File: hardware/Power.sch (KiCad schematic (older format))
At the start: 31 parts, among them J8 Batt, Q10 AO3401A, Q11 AO3400 (A09T), Q12 AO3401A, Q13 AO3400 (A09T), Q14 AO3400 (A09T), Q9 AO3400 (A09T), SW17 SW_SPDT, U1 TP4056, U3 DW-01, U8 HX9193-33GB

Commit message: Added dnp for battery charge circuit
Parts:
- C15, D17, D18, J8, Q10, Q11, Q12, Q13, Q14, Q9, R47, R48, R49, R50, R51, R52, R53, R54, R55, R56, R57, R58, SW17, U1, U3: dnp (none) -> y
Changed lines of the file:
@@
 F 8 "DW01" H 6700 4050 50  0001 L BNN "Field8"
 F 9 "C14213" H 6700 4050 50  0001 C CNN "LCSC"
+F 10 "y" H 6700 4050 50  0001 C CNN "dnp"
 	1    6700 4050
 	1    0    0    -1
@@
 F 3 "~" H 5800 3800 50  0001 C CNN
 F 4 "C23179" H 5800 3800 50  0001 C CNN "LCSC"
+F 5 "y" H 5800 3800 50  0001 C CNN "dnp"
 	1    5800 3800
 	0    1    1    0
@@
 F 3 "~" H 6150 3950 50  0001 C CNN
 F 4 "C14663" H 6150 3950 50  0001 C CNN "LCSC"
+F 5 "y" H 6150 3950 50  0001 C CNN "dnp"
 	1    6150 3950
 	1    0    0    -1
@@
 F 3 "http://www.aosmd.com/pdfs/datasheet/ao3400.pdf" H 6450 4850 50  0001 L CNN
 F 4 "C20917" H 6450 4850 50  0001 C CNN "LCSC"
+F 5 "y" H 6450 4850 50  0001 C CNN "dnp"
 	1    6450 4850
 	0    1    1    0
@@
 F 3 "http://www.aosmd.com/pdfs/datasheet/ao3400.pdf" H 6900 4850 50  0001 L CNN
 F 4 "C20917" H 6900 4850 50  0001 C CNN "LCSC"
+F 5 "y" H 6900 4850 50  0001 C CNN "dnp"
 	1    6900 4850
 	0    -1   1    0
@@
 F 3 "~" H 7200 4350 50  0001 C CNN
 F 4 "C21190" H 7200 4350 50  0001 C CNN "LCSC"
+F 5 "y" H 7200 4350 50  0001 C CNN "dnp"
 	1    7200 4350
 	-1   0    0    1
@@
 F 3 "http://www.aosmd.com/pdfs/datasheet/AO3401A.pdf" H 5150 2500 50  0001 L CNN
 F 4 "C15127" H 5150 2500 50  0001 C CNN "LCSC"
+F 5 "y" H 5150 2500 50  0001 C CNN "dnp"
 	1    5150 2500
 	0    -1   -1   0
@@
 F 3 "http://www.aosmd.com/pdfs/datasheet/AO3401A.pdf" H 5550 2500 50  0001 L CNN
 F 4 "C15127" H 5550 2500 50  0001 C CNN "LCSC"
+F 5 "y" H 5550 2500 50  0001 C CNN "dnp"
 	1    5550 2500
 	0    1    -1   0
@@
 F 3 "~" H 5000 2700 50  0001 C CNN
 F 4 "C25804" H 5000 2700 50  0001 C CNN "LCSC"
+F 5 "y" H 5000 2700 50  0001 C CNN "dnp"
 	1    5000 2700
 	0    1    -1   0
@@
 F 3 "https://dlnmh9ip6v2uc.cloudfront.net/datasheets/Prototyping/TP4056.pdf" H 3600 4150 60  0001 C CNN
 F 4 "C16581" H 3600 4150 50  0001 C CNN "LCSC"
+F 5 "y" H 3600 4150 50  0001 C CNN "dnp"
 	1    3600 4150
 	1    0    0    -1
@@
 F 3 "~" H 4100 4450 50  0001 C CNN
 F 4 "C22765" H 4100 4450 50  0001 C CNN "LCSC"
+F 5 "y" H 4100 4450 50  0001 C CNN "dnp"
 	1    4100 4450
 	1    0    0    -1
@@
 F 3 "~" H 2550 4600 50  0001 C CNN
 F 4 "C72043" H 2550 4600 50  0001 C CNN "LCSC"
+F 5 "y" H 2550 4600 50  0001 C CNN "dnp"
 	1    2550 4600
 	-1   0    0    1
@@
 F 3 "~" H 2550 4500 50  0001 C CNN
 F 4 "C72043" H 2550 4500 50  0001 C CNN "LCSC"
+F 5 "y" H 2550 4500 50  0001 C CNN "dnp"
 	1    2550 4500
 	-1   0    0    1
@@
 F 3 "~" H 2850 4350 50  0001 C CNN
 F 4 "C25804" H 2850 4350 50  0001 C CNN "LCSC"
+F 5 "y" H 2850 4350 50  0001 C CNN "dnp"
 	1    2850 4350
 	-1   0    0    -1
@@
 F 3 "~" H 3000 4450 50  0001 C CNN
 F 4 "C25804" H 3000 4450 50  0001 C CNN "LCSC"
+F 5 "y" H 3000 4450 50  0001 C CNN "dnp"
 	1    3000 4450
 	1    0    0    -1
@@
 F 3 "~" H 2750 3850 50  0001 C CNN
 F 4 "C25804" H 2750 3850 50  0001 C CNN "LCSC"
+F 5 "y" H 2750 3850 50  0001 C CNN "dnp"
 	1    2750 3850
 	1    0    0    -1
@@
 F 3 "http://www.aosmd.com/pdfs/datasheet/ao3400.pdf" H 2300 3950 50  0001 L CNN
 F 4 "C20917" H 2300 3950 50  0001 C CNN "LCSC"
+F 5 "y" V 2300 3950 50  0001 C CNN "dnp"
 	1    2300 3950
 	0    1    -1   0
@@
 F 3 "~" H 1950 4000 50  0001 C CNN
 F 4 "C25804" H 1950 4000 50  0001 C CNN "LCSC"
+F 5 "y" H 1950 4000 50  0001 C CNN "dnp"
 	1    1950 4000
 	1    0    0    -1
@@
 F 3 "http://www.aosmd.com/pdfs/datasheet/ao3400.pdf" H 5150 4550 50  0001 L CNN
 F 4 "C20917" H 5150 4550 50  0001 C CNN "LCSC"
+F 5 "y" H 5150 4550 50  0001 C CNN "dnp"
 	1    5150 4550
 	-1   0    0    -1
@@
 F 3 "~" H 5450 4200 50  0001 C CNN
 F 4 "C25804" H 5450 4200 50  0001 C CNN "LCSC"
+F 5 "y" H 5450 4200 50  0001 C CNN "dnp"
 	1    5450 4200
 	-1   0    0    1
@@
 F 2 "Connector_JST:JST_PH_B3B-PH-SM4-TB_1x03-1MP_P2.00mm_Vertical" H 4850 4050 50  0001 C CNN
 F 3 "~" H 4850 4050 50  0001 C CNN
+F 4 "y" H 4850 4050 50  0001 C CNN "dnp"
 	1    4850 4050
 	-1   0    0    -1
@@
 F 3 "~" H 4350 4450 50  0001 C CNN
 F 4 "C21189" H 4350 4450 50  0001 C CNN "LCSC"
+F 5 "y" H 4350 4450 50  0001 C CNN "dnp"
 	1    4350 4450
 	1    0    0    -1
@@
 F 2 "Resistor_SMD:R_0603_1608Metric" V 4280 3950 50  0001 C CNN
 F 3 "~" H 4350 3950 50  0001 C CNN
+F 4 "y" H 4350 3950 50  0001 C CNN "dnp"
 	1    4350 3950
 	1    0    0    -1
@@
 F 2 "Resistor_SMD:R_0603_1608Metric" V 4430 4200 50  0001 C CNN
 F 3 "~" H 4500 4200 50  0001 C CNN
+F 4 "y" H 4500 4200 50  0001 C CNN "dnp"
 	1    4500 4200
 	0    1    1    0
@@
 F 2 "switch:sk-3296s" H 5550 3000 50  0001 C CNN
 F 3 "~" H 5550 3000 50  0001 C CNN
+F 4 "y" H 5550 3000 50  0001 C CNN "dnp"
 	1    5550 3000
 	0    1    1    0

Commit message: Value cleanup
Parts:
- U8: value HX9193-33GB -> HX9193-33GB
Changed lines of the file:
@@
 P 9550 5700
 F 0 "U8" H 9550 6067 50  0000 C CNN
-F 1 " HX9193-33GB" H 9550 5976 50  0000 C CNN
+F 1 "HX9193-33GB" H 9550 5976 50  0000 C CNN
 F 2 "Package_TO_SOT_SMD:SOT-23-5" H 9550 5300 50  0001 C CNN
 F 3 "" H 9300 5950 50  0001 C CNN

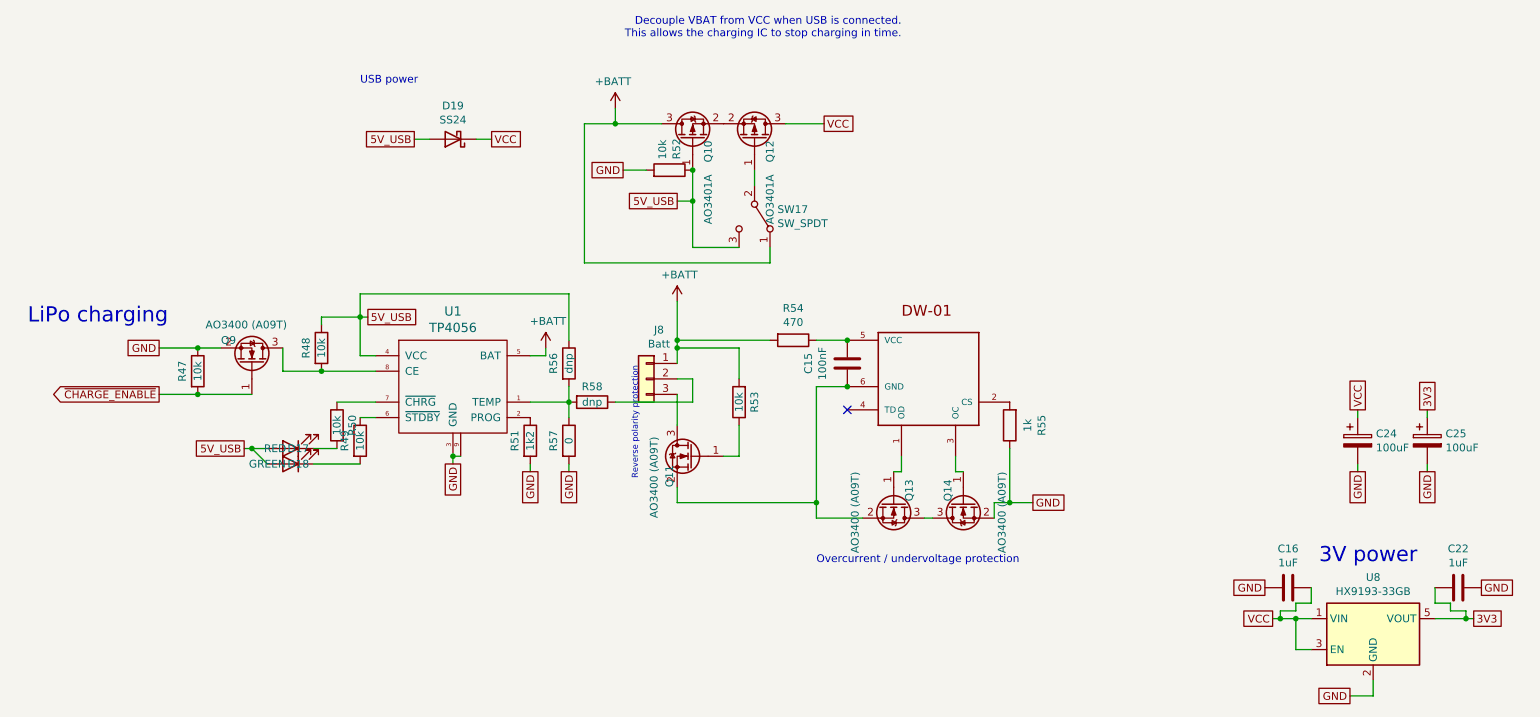
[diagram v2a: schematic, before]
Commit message: Added testpoints to audio lines
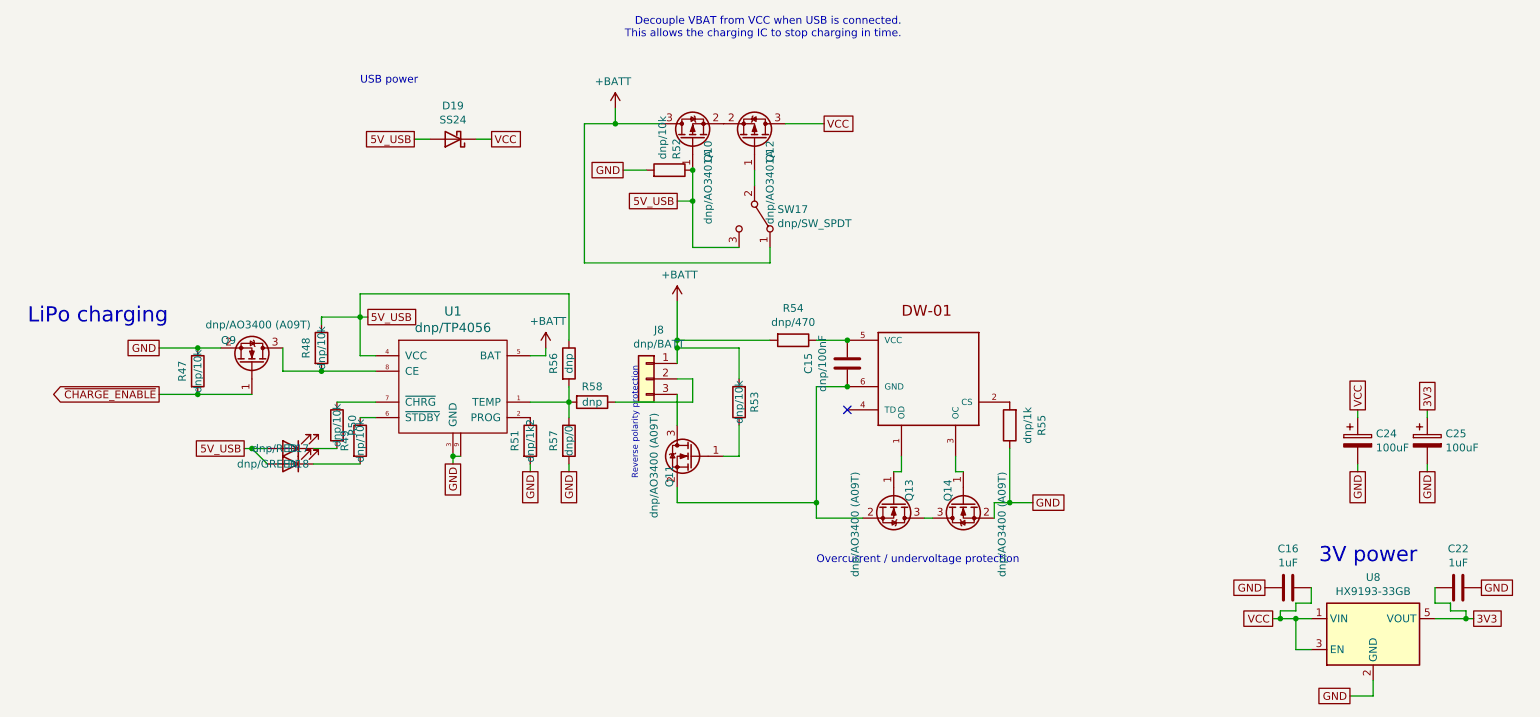
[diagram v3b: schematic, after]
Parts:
- C15: value 100nF -> dnp/100nF; LCSC C14663 -> (none)
- D17: value RED -> dnp/RED; LCSC C72043 -> (none)
- D18: value GREEN -> dnp/GREEN; LCSC C72043 -> (none)
- J8: value Batt -> dnp/BATT
- Q10, Q12: value AO3401A -> dnp/AO3401A; LCSC C15127 -> (none)
- Q11, Q13, Q14, Q9: value AO3400 (A09T) -> dnp/AO3400 (A09T); LCSC C20917 -> (none)
- R47, R48, R49, R50, R52, R53: value 10k -> dnp/10k; LCSC C25804 -> (none)
- R51: value 1k2 -> dnp/1k2; LCSC C22765 -> (none)
- R54: value 470 -> dnp/470; LCSC C23179 -> (none)
- R55: value 1k -> dnp/1k; LCSC C21190 -> (none)
- R57: value 0 -> dnp/0; LCSC C21189 -> (none)
- SW17: value SW_SPDT -> dnp/SW_SPDT
- U1: value TP4056 -> dnp/TP4056; LCSC C16581 -> (none)
- U3: value DW-01 -> dnp/DW-01; LCSC C14213 -> (none)
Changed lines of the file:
@@
 AR Path="/5E464BBE/5E449AD7" Ref="U3"  Part="1"
 F 0 "U3" H 6700 4050 50  0001 L BNN
-F 1 "DW-01" H 6700 4050 50  0001 L BNN
+F 1 "dnp/DW-01" H 6700 4050 50  0001 L BNN
 F 2 "Package_TO_SOT_SMD:SOT-23-6" H 6700 4050 50  0001 L BNN
 F 3 "1808 Murata Electronics" H 6700 4050 50  0001 L BNN
@@
 F 7 "Eldon Vloerstaande kasten DW - DW01" H 6700 4050 50  0001 L BNN "Field7"
 F 8 "DW01" H 6700 4050 50  0001 L BNN "Field8"
-F 9 "C14213" H 6700 4050 50  0001 C CNN "LCSC"
+F 9 "" H 6700 4050 50  0001 C CNN "LCSC"
 F 10 "y" H 6700 4050 50  0001 C CNN "dnp"
 	1    6700 4050
@@
 AR Path="/5E464BBE/5E449ADE" Ref="R54"  Part="1"
 F 0 "R54" V 5593 3800 50  0000 C CNN
-F 1 "470" V 5684 3800 50  0000 C CNN
+F 1 "dnp/470" V 5684 3800 50  0000 C CNN
 F 2 "Resistor_SMD:R_0603_1608Metric" V 5730 3800 50  0001 C CNN
 F 3 "~" H 5800 3800 50  0001 C CNN
-F 4 "C23179" H 5800 3800 50  0001 C CNN "LCSC"
+F 4 "" H 5800 3800 50  0001 C CNN "LCSC"
 F 5 "y" H 5800 3800 50  0001 C CNN "dnp"
 	1    5800 3800
@@
 AR Path="/5E464BBE/5E449AE7" Ref="C15"  Part="1"
 F 0 "C15" V 5898 3950 50  0000 C CNN
-F 1 "100nF" V 5989 3950 50  0000 C CNN
+F 1 "dnp/100nF" V 5989 3950 50  0000 C CNN
 F 2 "Capacitor_SMD:C_0603_1608Metric" H 6188 3800 50  0001 C CNN
 F 3 "~" H 6150 3950 50  0001 C CNN
-F 4 "C14663" H 6150 3950 50  0001 C CNN "LCSC"
+F 4 "" H 6150 3950 50  0001 C CNN "LCSC"
 F 5 "y" H 6150 3950 50  0001 C CNN "dnp"
 	1    6150 3950
@@
 AR Path="/5E464BBE/5E449AEF" Ref="Q13"  Part="1"
 F 0 "Q13" H 6300 4950 50  0000 L CNN
-F 1 "AO3400 (A09T)" H 6250 4600 50  0000 L CNN
+F 1 "dnp/AO3400 (A09T)" H 6250 4600 50  0000 L CNN
 F 2 "Package_TO_SOT_SMD:SOT-23" H 6650 4775 50  0001 L CIN
 F 3 "http://www.aosmd.com/pdfs/datasheet/ao3400.pdf" H 6450 4850 50  0001 L CNN
-F 4 "C20917" H 6450 4850 50  0001 C CNN "LCSC"
+F 4 "" H 6450 4850 50  0001 C CNN "LCSC"
 F 5 "y" H 6450 4850 50  0001 C CNN "dnp"
 	1    6450 4850
@@
 AR Path="/5E464BBE/5E449AF5" Ref="Q14"  Part="1"
 F 0 "Q14" H 6750 4950 50  0000 L CNN
-F 1 "AO3400 (A09T)" H 6700 4600 50  0000 L CNN
+F 1 "dnp/AO3400 (A09T)" H 6700 4600 50  0000 L CNN
 F 2 "Package_TO_SOT_SMD:SOT-23" H 7100 4775 50  0001 L CIN
 F 3 "http://www.aosmd.com/pdfs/datasheet/ao3400.pdf" H 6900 4850 50  0001 L CNN
-F 4 "C20917" H 6900 4850 50  0001 C CNN "LCSC"
+F 4 "" H 6900 4850 50  0001 C CNN "LCSC"
 F 5 "y" H 6900 4850 50  0001 C CNN "dnp"
 	1    6900 4850
@@
 AR Path="/5E464BBE/5E449B1C" Ref="R55"  Part="1"
 F 0 "R55" V 6993 4350 50  0000 C CNN
-F 1 "1k" V 7084 4350 50  0000 C CNN
+F 1 "dnp/1k" V 7084 4350 50  0000 C CNN
 F 2 "Resistor_SMD:R_0603_1608Metric" V 7130 4350 50  0001 C CNN
 F 3 "~" H 7200 4350 50  0001 C CNN
-F 4 "C21190" H 7200 4350 50  0001 C CNN "LCSC"
+F 4 "" H 7200 4350 50  0001 C CNN "LCSC"
 F 5 "y" H 7200 4350 50  0001 C CNN "dnp"
 	1    7200 4350
@@
 AR Path="/5E464BBE/5E45C88D" Ref="Q10"  Part="1"
 F 0 "Q10" H 5000 2400 50  0000 L CNN
-F 1 "AO3401A" H 4600 2400 50  0000 L CNN
+F 1 "dnp/AO3401A" H 4600 2400 50  0000 L CNN
 F 2 "Package_TO_SOT_SMD:SOT-23" H 5350 2425 50  0001 L CIN
 F 3 "http://www.aosmd.com/pdfs/datasheet/AO3401A.pdf" H 5150 2500 50  0001 L CNN
-F 4 "C15127" H 5150 2500 50  0001 C CNN "LCSC"
+F 4 "" H 5150 2500 50  0001 C CNN "LCSC"
 F 5 "y" H 5150 2500 50  0001 C CNN "dnp"
 	1    5150 2500
@@
 AR Path="/5E464BBE/5E45C893" Ref="Q12"  Part="1"
 F 0 "Q12" H 5400 2600 50  0000 L CNN
-F 1 "AO3401A" H 5000 2600 50  0000 L CNN
+F 1 "dnp/AO3401A" H 5000 2600 50  0000 L CNN
 F 2 "Package_TO_SOT_SMD:SOT-23" H 5750 2425 50  0001 L CIN
 F 3 "http://www.aosmd.com/pdfs/datasheet/AO3401A.pdf" H 5550 2500 50  0001 L CNN
-F 4 "C15127" H 5550 2500 50  0001 C CNN "LCSC"
+F 4 "" H 5550 2500 50  0001 C CNN "LCSC"
 F 5 "y" H 5550 2500 50  0001 C CNN "dnp"
 	1    5550 2500
@@
 AR Path="/5E464BBE/5E45C8FB" Ref="R52"  Part="1"
 F 0 "R52" H 5070 2746 50  0000 L CNN
-F 1 "10k" H 5070 2655 50  0000 L CNN
+F 1 "dnp/10k" H 5070 2655 50  0000 L CNN
 F 2 "Resistor_SMD:R_0603_1608Metric" V 4930 2700 50  0001 C CNN
 F 3 "~" H 5000 2700 50  0001 C CNN
-F 4 "C25804" H 5000 2700 50  0001 C CNN "LCSC"
+F 4 "" H 5000 2700 50  0001 C CNN "LCSC"
 F 5 "y" H 5000 2700 50  0001 C CNN "dnp"
 	1    5000 2700
@@
 AR Path="/5E464BBE/5E4683C0" Ref="U1"  Part="1"
 F 0 "U1" H 3600 4687 60  0000 C CNN
-F 1 "TP4056" H 3600 4581 60  0000 C CNN
+F 1 "dnp/TP4056" H 3600 4581 60  0000 C CNN
 F 2 "Package_SO:SOIC-8-1EP_3.9x4.9mm_P1.27mm_EP2.29x3mm" H 3600 4150 60  0001 C CNN
 F 3 "https://dlnmh9ip6v2uc.cloudfront.net/datasheets/Prototyping/TP4056.pdf" H 3600 4150 60  0001 C CNN
-F 4 "C16581" H 3600 4150 50  0001 C CNN "LCSC"
+F 4 "" H 3600 4150 50  0001 C CNN "LCSC"
 F 5 "y" H 3600 4150 50  0001 C CNN "dnp"
 	1    3600 4150
@@
 AR Path="/5E464BBE/5E4683C8" Ref="R51"  Part="1"
 F 0 "R51" V 4000 4450 50  0000 C CNN
-F 1 "1k2" V 4100 4450 50  0000 C CNN
+F 1 "dnp/1k2" V 4100 4450 50  0000 C CNN
 F 2 "Resistor_SMD:R_0603_1608Metric" V 4030 4450 50  0001 C CNN
 F 3 "~" H 4100 4450 50  0001 C CNN
-F 4 "C22765" H 4100 4450 50  0001 C CNN "LCSC"
+F 4 "" H 4100 4450 50  0001 C CNN "LCSC"
 F 5 "y" H 4100 4450 50  0001 C CNN "dnp"
 	1    4100 4450
@@
 AR Path="/5E464BBE/5E4683D9" Ref="D17"  Part="1"
 F 0 "D17" H 2500 4500 50  0000 C CNN
-F 1 "RED" H 2650 4500 50  0000 C CNN
+F 1 "dnp/RED" H 2650 4500 50  0000 C CNN
 F 2 "LED_SMD:LED_0603_1608Metric" H 2550 4600 50  0001 C CNN
 F 3 "~" H 2550 4600 50  0001 C CNN
-F 4 "C72043" H 2550 4600 50  0001 C CNN "LCSC"
+F 4 "" H 2550 4600 50  0001 C CNN "LCSC"
 F 5 "y" H 2550 4600 50  0001 C CNN "dnp"
 	1    2550 4600
@@
 AR Path="/5E464BBE/5E4683DF" Ref="D18"  Part="1"
 F 0 "D18" H 2500 4600 50  0000 C CNN
-F 1 "GREEN" H 2700 4600 50  0000 C CNN
+F 1 "dnp/GREEN" H 2700 4600 50  0000 C CNN
 F 2 "LED_SMD:LED_0603_1608Metric" H 2550 4500 50  0001 C CNN
 F 3 "~" H 2550 4500 50  0001 C CNN
-F 4 "C72043" H 2550 4500 50  0001 C CNN "LCSC"
+F 4 "" H 2550 4500 50  0001 C CNN "LCSC"
 F 5 "y" H 2550 4500 50  0001 C CNN "dnp"
 	1    2550 4500
@@
 AR Path="/5E464BBE/5E4683E7" Ref="R50"  Part="1"
 F 0 "R50" V 2750 4350 50  0000 C CNN
-F 1 "10k" V 2850 4350 50  0000 C CNN
+F 1 "dnp/10k" V 2850 4350 50  0000 C CNN
 F 2 "Resistor_SMD:R_0603_1608Metric" V 2780 4350 50  0001 C CNN
 F 3 "~" H 2850 4350 50  0001 C CNN
-F 4 "C25804" H 2850 4350 50  0001 C CNN "LCSC"
+F 4 "" H 2850 4350 50  0001 C CNN "LCSC"
 F 5 "y" H 2850 4350 50  0001 C CNN "dnp"
 	1    2850 4350
@@
 AR Path="/5E464BBE/5E4683ED" Ref="R49"  Part="1"
 F 0 "R49" V 2900 4450 50  0000 C CNN
-F 1 "10k" V 3000 4450 50  0000 C CNN
+F 1 "dnp/10k" V 3000 4450 50  0000 C CNN
 F 2 "Resistor_SMD:R_0603_1608Metric" V 2930 4450 50  0001 C CNN
 F 3 "~" H 3000 4450 50  0001 C CNN
-F 4 "C25804" H 3000 4450 50  0001 C CNN "LCSC"
+F 4 "" H 3000 4450 50  0001 C CNN "LCSC"
 F 5 "y" H 3000 4450 50  0001 C CNN "dnp"
 	1    3000 4450
@@
 AR Path="/5E464BBE/5E4683FC" Ref="R48"  Part="1"
 F 0 "R48" V 2650 3850 50  0000 C CNN
-F 1 "10k" V 2750 3850 50  0000 C CNN
+F 1 "dnp/10k" V 2750 3850 50  0000 C CNN
 F 2 "Resistor_SMD:R_0603_1608Metric" V 2680 3850 50  0001 C CNN
 F 3 "~" H 2750 3850 50  0001 C CNN
-F 4 "C25804" H 2750 3850 50  0001 C CNN "LCSC"
+F 4 "" H 2750 3850 50  0001 C CNN "LCSC"
 F 5 "y" H 2750 3850 50  0001 C CNN "dnp"
 	1    2750 3850
@@
 AR Path="/5E464BBE/5E468407" Ref="Q9"  Part="1"
 F 0 "Q9" V 2450 3750 50  0000 L CNN
-F 1 "AO3400 (A09T)" V 2550 3650 50  0000 L CNN
+F 1 "dnp/AO3400 (A09T)" V 2550 3650 50  0000 L CNN
 F 2 "Package_TO_SOT_SMD:SOT-23" H 2500 3875 50  0001 L CIN
 F 3 "http://www.aosmd.com/pdfs/datasheet/ao3400.pdf" H 2300 3950 50  0001 L CNN
-F 4 "C20917" H 2300 3950 50  0001 C CNN "LCSC"
+F 4 "" H 2300 3950 50  0001 C CNN "LCSC"
 F 5 "y" V 2300 3950 50  0001 C CNN "dnp"
 	1    2300 3950
@@
 AR Path="/5E464BBE/5E46841A" Ref="R47"  Part="1"
 F 0 "R47" V 1850 4000 50  0000 C CNN
-F 1 "10k" V 1950 4000 50  0000 C CNN
+F 1 "dnp/10k" V 1950 4000 50  0000 C CNN
 F 2 "Resistor_SMD:R_0603_1608Metric" V 1880 4000 50  0001 C CNN
 F 3 "~" H 1950 4000 50  0001 C CNN
-F 4 "C25804" H 1950 4000 50  0001 C CNN "LCSC"
+F 4 "" H 1950 4000 50  0001 C CNN "LCSC"
 F 5 "y" H 1950 4000 50  0001 C CNN "dnp"
 	1    1950 4000
@@
 P 5150 4550
 F 0 "Q11" V 5300 4350 50  0000 L CNN
-F 1 "AO3400 (A09T)" V 5400 4150 50  0000 L CNN
+F 1 "dnp/AO3400 (A09T)" V 5400 4150 50  0000 L CNN
 F 2 "Package_TO_SOT_SMD:SOT-23" H 5350 4475 50  0001 L CIN
 F 3 "http://www.aosmd.com/pdfs/datasheet/ao3400.pdf" H 5150 4550 50  0001 L CNN
-F 4 "C20917" H 5150 4550 50  0001 C CNN "LCSC"
+F 4 "" H 5150 4550 50  0001 C CNN "LCSC"
 F 5 "y" H 5150 4550 50  0001 C CNN "dnp"
 	1    5150 4550
@@
 P 5450 4200
 F 0 "R53" V 5350 4200 50  0000 C CNN
-F 1 "10k" V 5450 4200 50  0000 C CNN
+F 1 "dnp/10k" V 5450 4200 50  0000 C CNN
 F 2 "Resistor_SMD:R_0603_1608Metric" V 5380 4200 50  0001 C CNN
 F 3 "~" H 5450 4200 50  0001 C CNN
-F 4 "C25804" H 5450 4200 50  0001 C CNN "LCSC"
+F 4 "" H 5450 4200 50  0001 C CNN "LCSC"
 F 5 "y" H 5450 4200 50  0001 C CNN "dnp"
 	1    5450 4200
@@
 P 4850 4050
 F 0 "J8" H 4768 4367 50  0000 C CNN
-F 1 "Batt" H 4768 4276 50  0000 C CNN
+F 1 "dnp/BATT" H 4768 4276 50  0000 C CNN
 F 2 "Connector_JST:JST_PH_B3B-PH-SM4-TB_1x03-1MP_P2.00mm_Vertical" H 4850 4050 50  0001 C CNN
 F 3 "~" H 4850 4050 50  0001 C CNN
@@
 AR Path="/5E464BBE/5E811481" Ref="R57"  Part="1"
 F 0 "R57" V 4250 4450 50  0000 C CNN
-F 1 "0" V 4350 4450 50  0000 C CNN
+F 1 "dnp/0" V 4350 4450 50  0000 C CNN
 F 2 "Resistor_SMD:R_0603_1608Metric" V 4280 4450 50  0001 C CNN
 F 3 "~" H 4350 4450 50  0001 C CNN
-F 4 "C21189" H 4350 4450 50  0001 C CNN "LCSC"
+F 4 "" H 4350 4450 50  0001 C CNN "LCSC"
 F 5 "y" H 4350 4450 50  0001 C CNN "dnp"
 	1    4350 4450
@@
 P 5550 3000
 F 0 "SW17" V 5504 3148 50  0000 L CNN
-F 1 "SW_SPDT" V 5595 3148 50  0000 L CNN
+F 1 "dnp/SW_SPDT" V 5595 3148 50  0000 L CNN
 F 2 "switch:sk-3296s" H 5550 3000 50  0001 C CNN
 F 3 "~" H 5550 3000 50  0001 C CNN
